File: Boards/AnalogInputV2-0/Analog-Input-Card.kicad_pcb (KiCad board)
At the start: 2 copper layers, 80 x 72 mm, 62 parts, among them IC1 PIC32MM0064GPM028, P1 6x1 2.54, P1 AquaPicBus, P2 2@ 8x1 2.54, P3 2x1 2.54, P4 2x1 2.54, Q1 AO3407A, Q2 NX7002AK, Q3 NX7002AK, Q4 NX7002AK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

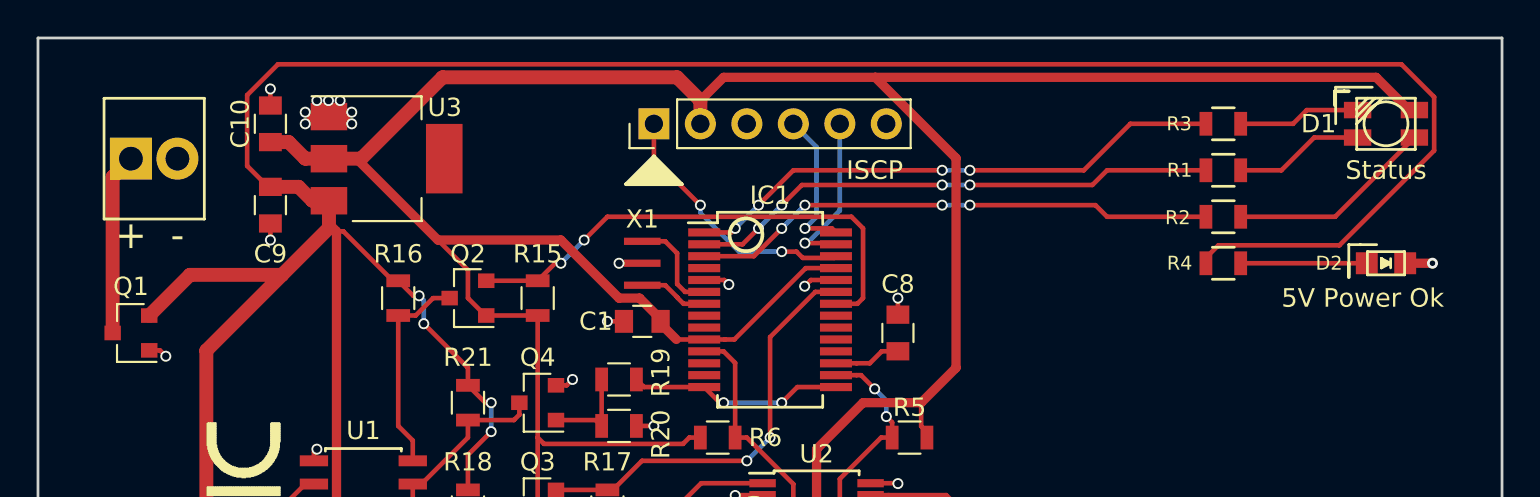
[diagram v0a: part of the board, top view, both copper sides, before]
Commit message: added firmware for the pH ORP Card
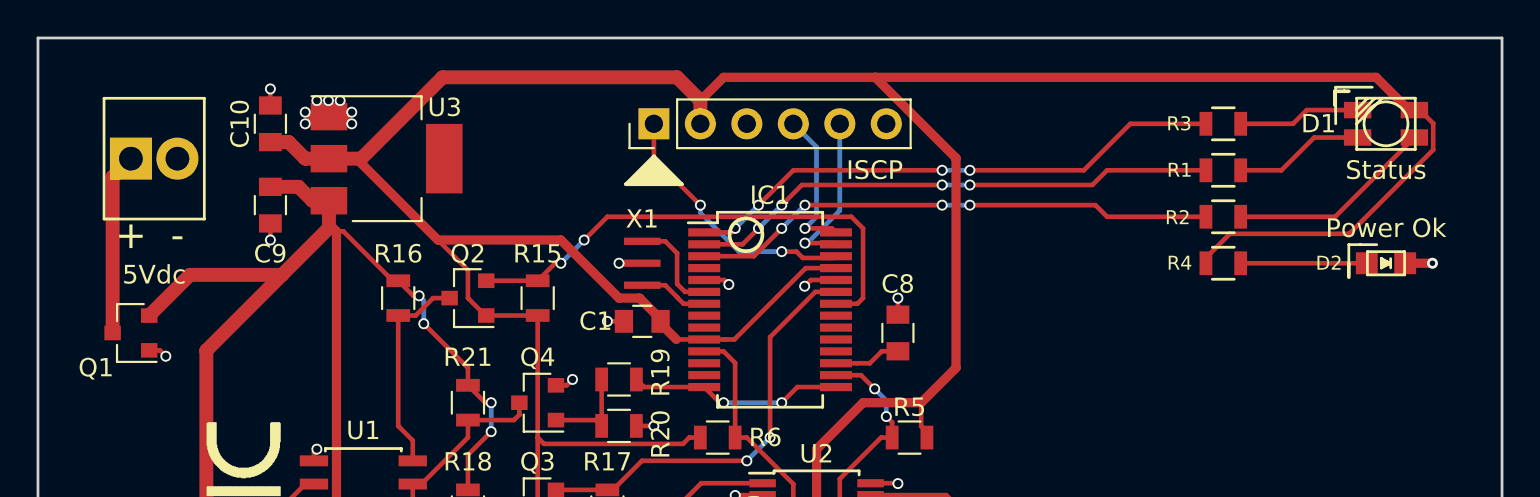
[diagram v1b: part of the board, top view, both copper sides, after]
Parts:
- renumbered P4 to 5Vdc
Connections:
- R4 pad 1: +5V -> +3V3
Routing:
- net +5V: track 251.4 -> 161.2 mm
- net +3V3: track 171.9 -> 189.8 mm
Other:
- board text added: "AquaPic Analog Input Rev 2 Goodtime Development Skyler Brandt"
- board text added: "Power Ok"
- board text removed: "5V Power Ok"
- board text removed: "AquaPic Analog Input Rev 2.0 Goodtime Development"
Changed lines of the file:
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@@
     (thickness 1.6)
     (drawings 57)
-    (tracks 511)
+    (tracks 507)
     (zones 0)
     (modules 62)
@@
     (mod_text_size 1 1)
     (mod_text_width 0.15)
-    (pad_size 1 1.25)
+    (pad_size 0.7 1.3)
     (pad_drill 0)
     (pad_to_mask_clearance 0.2)
@@
     (fp_line (start -0.6 -0.875) (end 0.6 -0.875) (layer F.SilkS) (width 0.15))
     (pad 1 smd rect (at -0.95 0) (size 0.7 1.3) (layers F.Cu F.Paste F.Mask)
-      (net 1 +5V))
+      (net 34 +3V3))
     (pad 2 smd rect (at 0.95 0) (size 0.7 1.3) (layers F.Cu F.Paste F.Mask)
       (net 6 "Net-(D2-Pad1)"))
@@
   (module MyFootPrints:Screw_Header_1x2 (layer F.Cu)
     (at 6.35 -65.405)
-    (fp_text reference P4 (at -1.27 -2.159) (layer F.SilkS) hide
-      (effects (font (size 1.5 1.5) (thickness 0.15)))
+    (fp_text reference 5Vdc (at 0 6.35) (layer F.SilkS)
+      (effects (font (size 1.016 1.016) (thickness 0.15)))
     )
     (fp_text value "2x1 2.54 " (at 0 0) (layer F.Fab)
@@
     (tags SOT-23)
     (attr smd)
-    (fp_text reference Q1 (at 0 2.54 180) (layer F.SilkS)
+    (fp_text reference Q1 (at 1.905 -1.905 180) (layer F.SilkS)
       (effects (font (size 1 1) (thickness 0.15)))
     )
@@
   (gr_circle (center 18.415 -45.593) (end 19.05 -44.958) (layer F.SilkS) (width 0.2))
   (gr_circle (center 39.116 -45.983025) (end 39.751 -45.348025) (layer F.SilkS) (width 0.2))
-  (gr_text "AquaPic\nAnalog Input\nRev 2.0\nGoodtime Development" (at 64.77 -24.765) (layer B.SilkS)
+  (gr_text "AquaPic\nAnalog Input\nRev 2\nGoodtime Development\nSkyler Brandt" (at 65.405 -24.765) (layer B.SilkS)
     (effects (font (size 1.016 1.016) (thickness 0.1524)) (justify mirror))
   )
@@
     (effects (font (size 1.27 1.27) (thickness 0.2032)))
   )
-  (gr_text "5V Power Ok" (at 72.39 -57.785) (layer F.SilkS)
-    (effects (font (size 1.016 1.016) (thickness 0.2032)))
+  (gr_text "Power Ok" (at 73.66 -61.595) (layer F.SilkS)
+    (effects (font (size 1.016 1.016) (thickness 0.1524)))
   )
   (gr_text Status (at 73.66 -64.77) (layer F.SilkS)
-    (effects (font (size 1.016 1.016) (thickness 0.2032)))
+    (effects (font (size 1.016 1.016) (thickness 0.1524)))
   )
   (gr_text - (at 7.62 -61.214) (layer F.SilkS)
@@
   (via (at 24.765 -50.4898) (size 0.6) (drill 0.4) (layers F.Cu B.Cu) (net 1))
   (segment (start 12.7 -63.865) (end 12.575 -63.865) (width 0.254) (layer F.Cu) (net 1))
-  (segment (start 74.503152 -70.56121) (end 76.290201 -68.774161) (width 0.254) (layer F.Cu) (net 1))
-  (segment (start 12.575 -63.865) (end 11.43 -65.01) (width 0.254) (layer F.Cu) (net 1))
-  (segment (start 11.43 -65.01) (end 11.43 -68.877698) (width 0.254) (layer F.Cu) (net 1))
-  (segment (start 76.290201 -65.845839) (end 71.114563 -60.670201) (width 0.254) (layer F.Cu) (net 1))
-  (segment (start 63.82 -59.99) (end 63.82 -59.69) (width 0.254) (layer F.Cu) (net 1))
-  (segment (start 11.43 -68.877698) (end 13.113512 -70.56121) (width 0.254) (layer F.Cu) (net 1))
-  (segment (start 13.113512 -70.56121) (end 74.503152 -70.56121) (width 0.254) (layer F.Cu) (net 1))
-  (segment (start 76.290201 -68.774161) (end 76.290201 -65.845839) (width 0.254) (layer F.Cu) (net 1))
-  (segment (start 71.114563 -60.670201) (end 64.500201 -60.670201) (width 0.254) (layer F.Cu) (net 1))
-  (segment (start 64.500201 -60.670201) (end 63.82 -59.99) (width 0.254) (layer F.Cu) (net 1))
   (segment (start 16.312201 -61.434799) (end 16.685201 -61.434799) (width 0.254) (layer F.Cu) (net 1))
   (segment (start 16.685201 -61.434799) (end 19.385 -58.735) (width 0.254) (layer F.Cu) (net 1))
@@
   (segment (start 24.765 -3.81) (end 32.385 -3.81) (width 0.762) (layer F.Cu) (net 1))
   (segment (start 23.495 -5.08) (end 24.765 -3.81) (width 0.762) (layer F.Cu) (net 1))
-  (segment (start 63.82 -59.69) (end 63.82 -60.01) (width 0.254) (layer F.Cu) (net 1))
   (segment (start 9.2 -18.805005) (end 9.2 -16.185005) (width 0.762) (layer F.Cu) (net 1))
   (segment (start 15.08 -48.895) (end 15.08 -49.37) (width 0.254) (layer F.Cu) (net 2))
@@
   (segment (start 59.055 -28.575) (end 59.055 -31.5595) (width 0.254) (layer F.Cu) (net 33))
   (segment (start 61.595 -26.8605) (end 60.7695 -26.8605) (width 0.254) (layer F.Cu) (net 33))
+  (segment (start 63.82 -59.69) (end 63.82 -59.99) (width 0.254) (layer F.Cu) (net 34))
+  (segment (start 63.82 -59.99) (end 65.130599 -61.300599) (width 0.254) (layer F.Cu) (net 34))
+  (segment (start 65.130599 -61.300599) (end 71.653521 -61.300599) (width 0.254) (layer F.Cu) (net 34))
+  (segment (start 71.653521 -61.300599) (end 76.239401 -65.886479) (width 0.254) (layer F.Cu) (net 34))
+  (segment (start 75.51 -68.06) (end 75.21 -68.06) (width 0.254) (layer F.Cu) (net 34))
+  (segment (start 76.239401 -65.886479) (end 76.239401 -67.330599) (width 0.254) (layer F.Cu) (net 34))
+  (segment (start 76.239401 -67.330599) (end 75.51 -68.06) (width 0.254) (layer F.Cu) (net 34))
   (segment (start 43.605 -59.425) (end 41.952064 -59.425) (width 0.254) (layer F.Cu) (net 34))
   (segment (start 41.952064 -59.425) (end 38.052064 -55.525) (width 0.254) (layer F.Cu) (net 34))

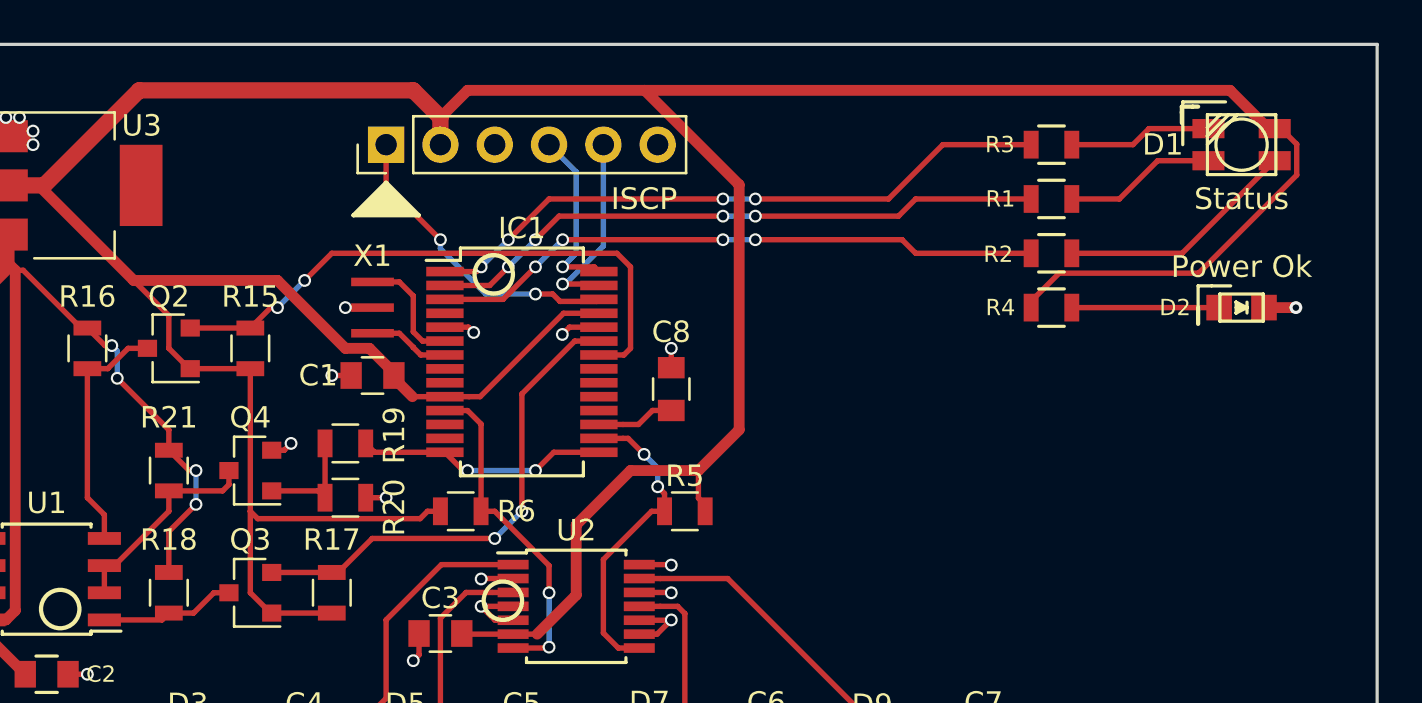
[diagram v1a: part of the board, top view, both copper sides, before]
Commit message: fixed pinout on analog input card
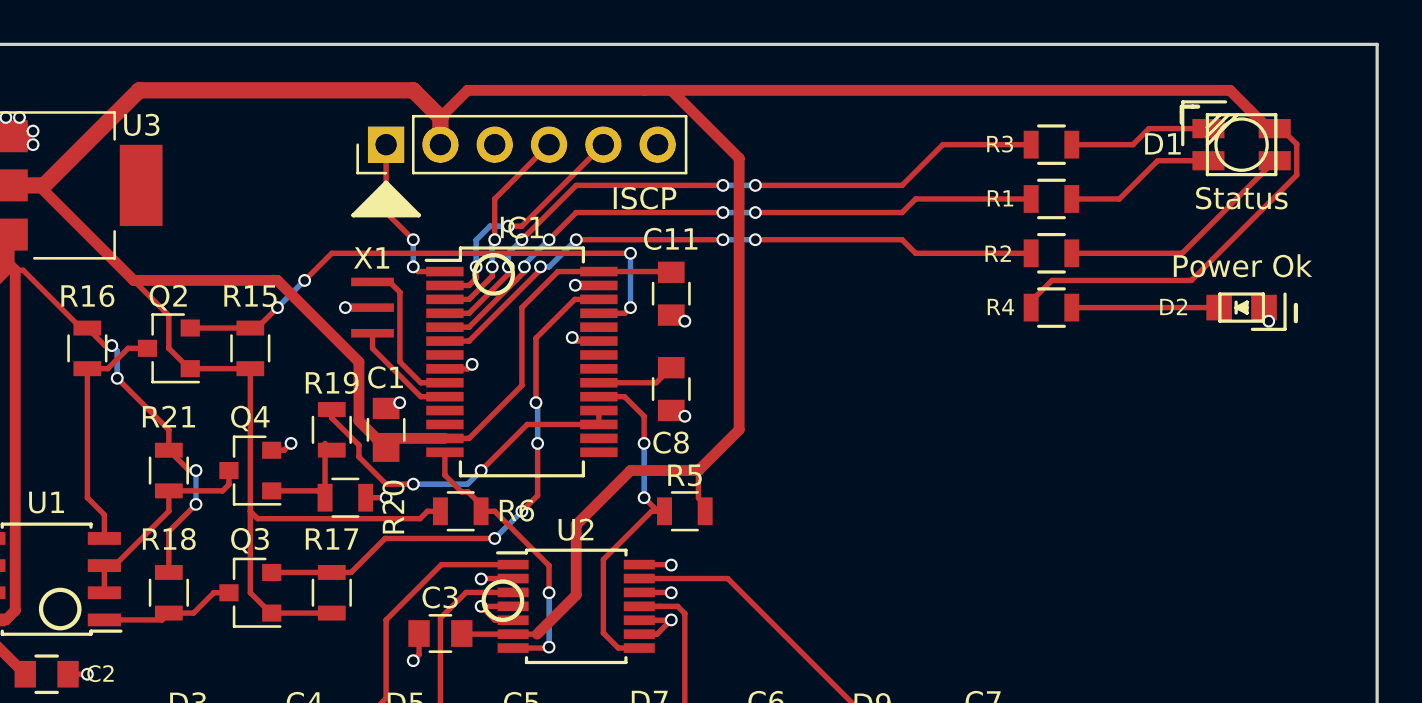
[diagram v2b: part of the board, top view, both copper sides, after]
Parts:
- added C11: 100nF, Capacitors_SMD:C_0805, F.Cu at (47.0, -60.3)
- D1: value SMP4-RGY -> SMTL4-RGY
- P2: value 2@ 8x1 2.54 -> Inputs
- P3: value 2x1 2.54 -> Earth
- R1, R2, R3, R4: value 300R -> 150R
- moved C1 2.62 mm to (33.7, -54.0), turned to 90 degrees
- moved R19 0.90 mm to (31.1, -54.0), turned to 90 degrees
- turned C8 to 270 degrees
- turned D2 to 180 degrees
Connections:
- D2 pad 1: Net-(D2-Pad1) -> GND
- D2 pad 2: GND -> Net-(D2-Pad2)
- IC1 pad 1: /LED_R -> //MCLR
- IC1 pad 10: +3V3 -> Net-(IC1-Pad10)
- IC1 pad 11: /SDA -> Net-(IC1-Pad11)
- IC1 pad 13: Net-(IC1-Pad13) -> +3V3
- IC1 pad 14: //RTS -> /SDA
- IC1 pad 15: //RTS -> Net-(IC1-Pad15)
- IC1 pad 16: /SCL -> Net-(IC1-Pad16)
- IC1 pad 17: Net-(C8-Pad1) -> //RTS
- IC1 pad 18: Net-(IC1-Pad18) -> //RTS
- IC1 pad 19: Net-(IC1-Pad19) -> /SCL
- IC1 pad 2: /LED_G -> /PGC
- IC1 pad 20: Net-(IC1-Pad20) -> Net-(C8-Pad1)
- IC1 pad 22: /TX_LV -> Net-(IC1-Pad22)
- IC1 pad 23: /RX_LV -> GND
- IC1 pad 24: GND -> Net-(IC1-Pad24)
- IC1 pad 25: +3V3 -> /TX_LV
- IC1 pad 26: //MCLR -> /RX_LV
- IC1 pad 27: /PGC -> GND
- IC1 pad 28: /PGD -> +3V3
- IC1 pad 3: /LED_Y -> /PGD
- IC1 pad 4: Net-(IC1-Pad4) -> /LED_R
- IC1 pad 5: GND -> /LED_G
- IC1 pad 6: Net-(IC1-Pad6) -> /LED_Y
- IC1 pad 8: Net-(IC1-Pad8) -> GND
- R4 pad 2: Net-(D2-Pad1) -> Net-(D2-Pad2)
- X1 pad 1: Net-(IC1-Pad7) -> Net-(IC1-Pad10)
- X1 pad 3: Net-(IC1-Pad6) -> Net-(IC1-Pad9)
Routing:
- net +3V3: track 189.8 -> 199.3 mm
- net Net-(IC1-Pad9): track 0.00 -> 7.25 mm
- net Net-(D2-Pad2): track 0.00 -> 6.89 mm
- net Net-(D2-Pad1): track 6.89 -> 0.00 mm
- net //MCLR: track 14.4 -> 7.81 mm
- net Net-(IC1-Pad6): track 5.51 -> 0.00 mm
- net Net-(IC1-Pad10): track 0.00 -> 5.03 mm
- net //RTS: track 12.4 -> 16.3 mm
- net Net-(IC1-Pad7): track 3.81 -> 0.00 mm
- net /RX_LV: track 23.0 -> 25.4 mm, vias 2 -> 4
- net /PGC: track 9.11 -> 11.2 mm, vias 1 -> 2
- net /SCL: track 14.7 -> 16.7 mm
- net /SDA: track 15.8 -> 14.0 mm
- net /PGD: track 8.29 -> 9.91 mm, vias 1 -> 2
- net /TX_LV: track 27.7 -> 26.2 mm, vias 2 -> 4
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
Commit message: working on Analog Output card
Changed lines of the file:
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@@
   (gr_line (start 76.2 -59.055) (end 76.2 -59.817) (angle 90) (layer F.SilkS) (width 0.2))
   (gr_circle (center 18.415 -45.593) (end 19.05 -44.958) (layer F.SilkS) (width 0.2))
-  (gr_circle (center 39.116 -45.983025) (end 39.751 -45.348025) (layer F.SilkS) (width 0.2))
+  (gr_circle (center 41.529 -47.244) (end 42.164 -46.609) (layer F.SilkS) (width 0.2))
   (gr_text "AquaPic\nAnalog Input\nRev 2\nGoodtime Development\nSkyler Brandt" (at 65.405 -24.765) (layer B.SilkS)
     (effects (font (size 1.016 1.016) (thickness 0.1524)) (justify mirror))

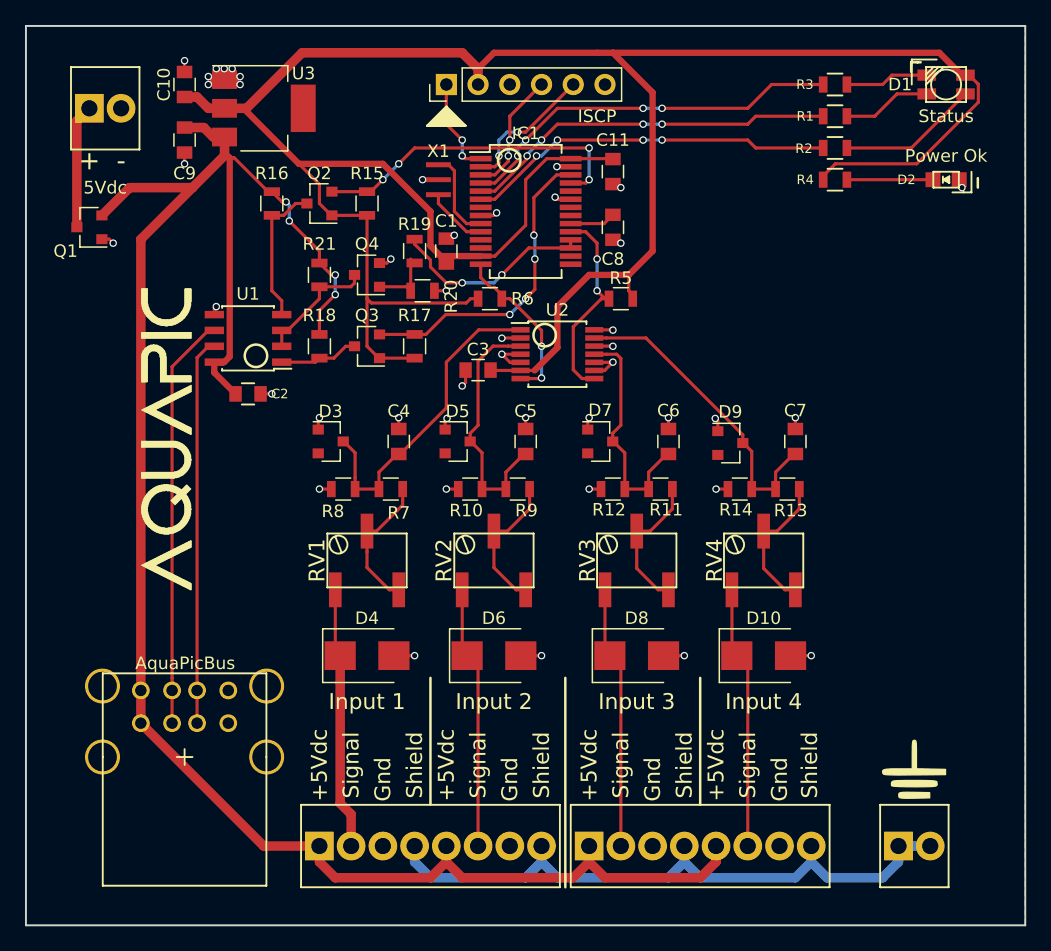
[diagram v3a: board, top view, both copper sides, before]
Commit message: fixed placement on boards so everything is mostly in the same spot
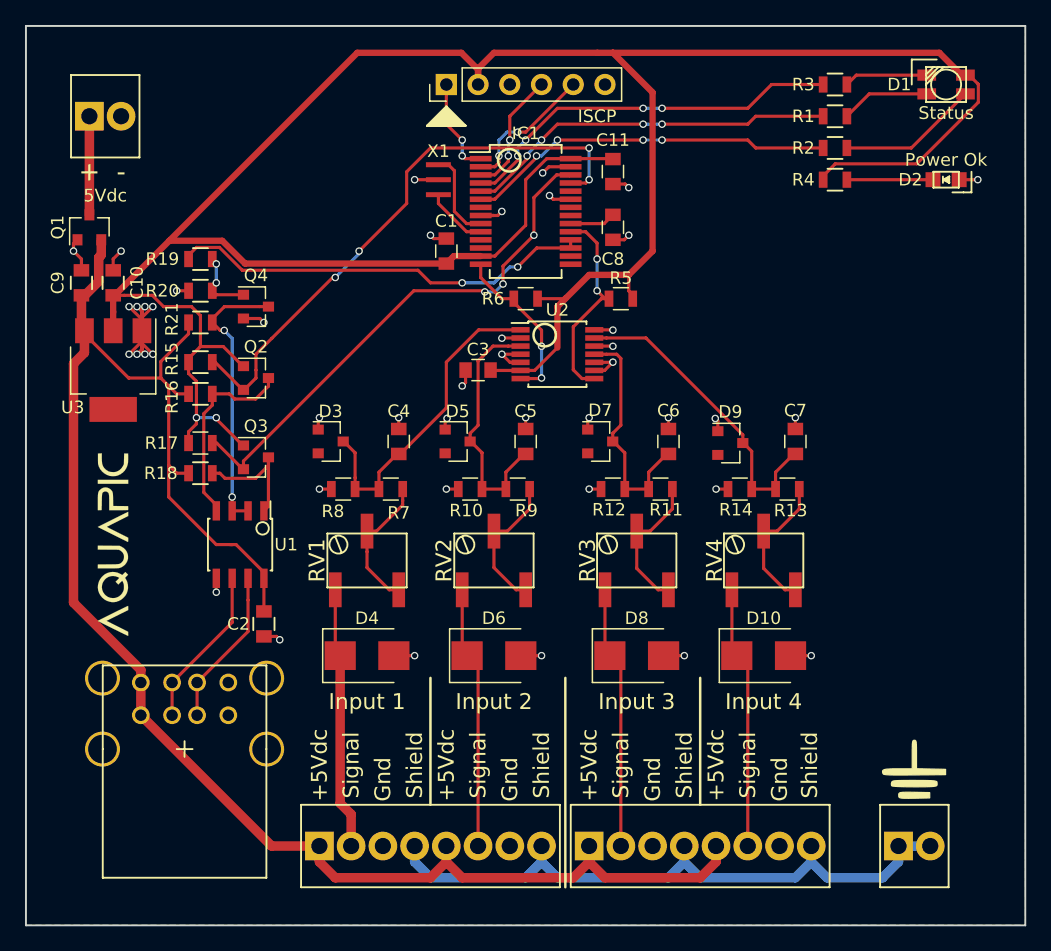
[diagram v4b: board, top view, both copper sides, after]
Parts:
- removed ?: , Symbols:Symbol_OSHW-Logo_SilkScreen
- removed LOGO: Val**, A_MyFootPrints:AquaPic_Logo
- added G***: LOGO, MyFootPrints:AquaPic_Logo_Small, F.Cu at (6.99, -30.5)
- added REF***: OSHW-Logo2_14.6x12mm_SilkScreen, Symbols:OSHW-Logo2_14.6x12mm_SilkScreen, B.Cu at (54.0, -25.4)
- 5Vdc: value 2x1 2.54 -> 2x1 2.54
- P1: value AquaPicBus -> usb1.1
- moved U3 24.2 mm to (6.99, -44.5), turned to 270 degrees
- moved R17 18.8 mm to (14.0, -38.6), turned to 0 degrees
- moved C2 18.5 mm to (19.1, -24.1), turned to 270 degrees
- moved R15 18.4 mm to (14.0, -45.1), turned to 0 degrees
- moved R20 17.8 mm to (14.0, -50.8), turned to 180 degrees
- moved R19 17.2 mm to (14.0, -53.3), turned to 180 degrees
- moved C10 16.9 mm to (6.99, -51.4)
- moved U1 16.5 mm to (17.1, -30.5), turned to 270 degrees
- moved R16 16.3 mm to (14.0, -42.5), turned to 0 degrees
- moved Q2 14.9 mm to (18.4, -43.8), turned to 0 degrees
- moved C9 14.1 mm to (4.45, -51.4), turned to 90 degrees
- moved R18 13.9 mm to (14.0, -36.2), turned to 0 degrees
- moved Q3 12.6 mm to (18.4, -37.5), turned to 0 degrees
- moved R21 10.3 mm to (14.0, -48.3), turned to 0 degrees
- moved Q4 9.25 mm to (18.4, -49.5), turned to 0 degrees
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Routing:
- net +5V: track 161.2 -> 140.3 mm, vias 4 -> 0
- net /A: track 33.1 -> 13.0 mm
- net /TX_LV: track 26.2 -> 46.0 mm
- net GND: track 53.9 -> 73.4 mm
- net //RTS: track 16.3 -> 35.0 mm
- net /B: track 31.0 -> 12.6 mm
- net /RX_LV: track 25.4 -> 42.6 mm, vias 4 -> 3
- net +3V3: track 199.3 -> 212.3 mm, vias 0 -> 2
- net /RTS: track 9.88 -> 22.4 mm, vias 0 -> 2
- net /TX: track 11.5 -> 15.8 mm
- net /RX: track 6.35 -> 10.2 mm
- net Net-(P3-Pad1): track 9.94 -> 7.89 mm
- net Net-(Q1-Pad1): track 5.17 -> 5.43 mm, vias 0 -> 2
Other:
- board text added: "AquaPic Analog Input Rev 2.0 Goodtime Development Skyler Brandt"
- board text removed: "AquaPic Analog Input Rev 2 Goodtime Development Skyler Brandt"

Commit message: more work on uniformity between boards
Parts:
- moved P2 0.64 mm to (43.2, -6.99)
- moved P3 0.64 mm to (71.1, -6.99)
- moved G*** 0.63 mm to (71.1, -12.1)
